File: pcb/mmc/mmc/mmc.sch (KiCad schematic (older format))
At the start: 1 part

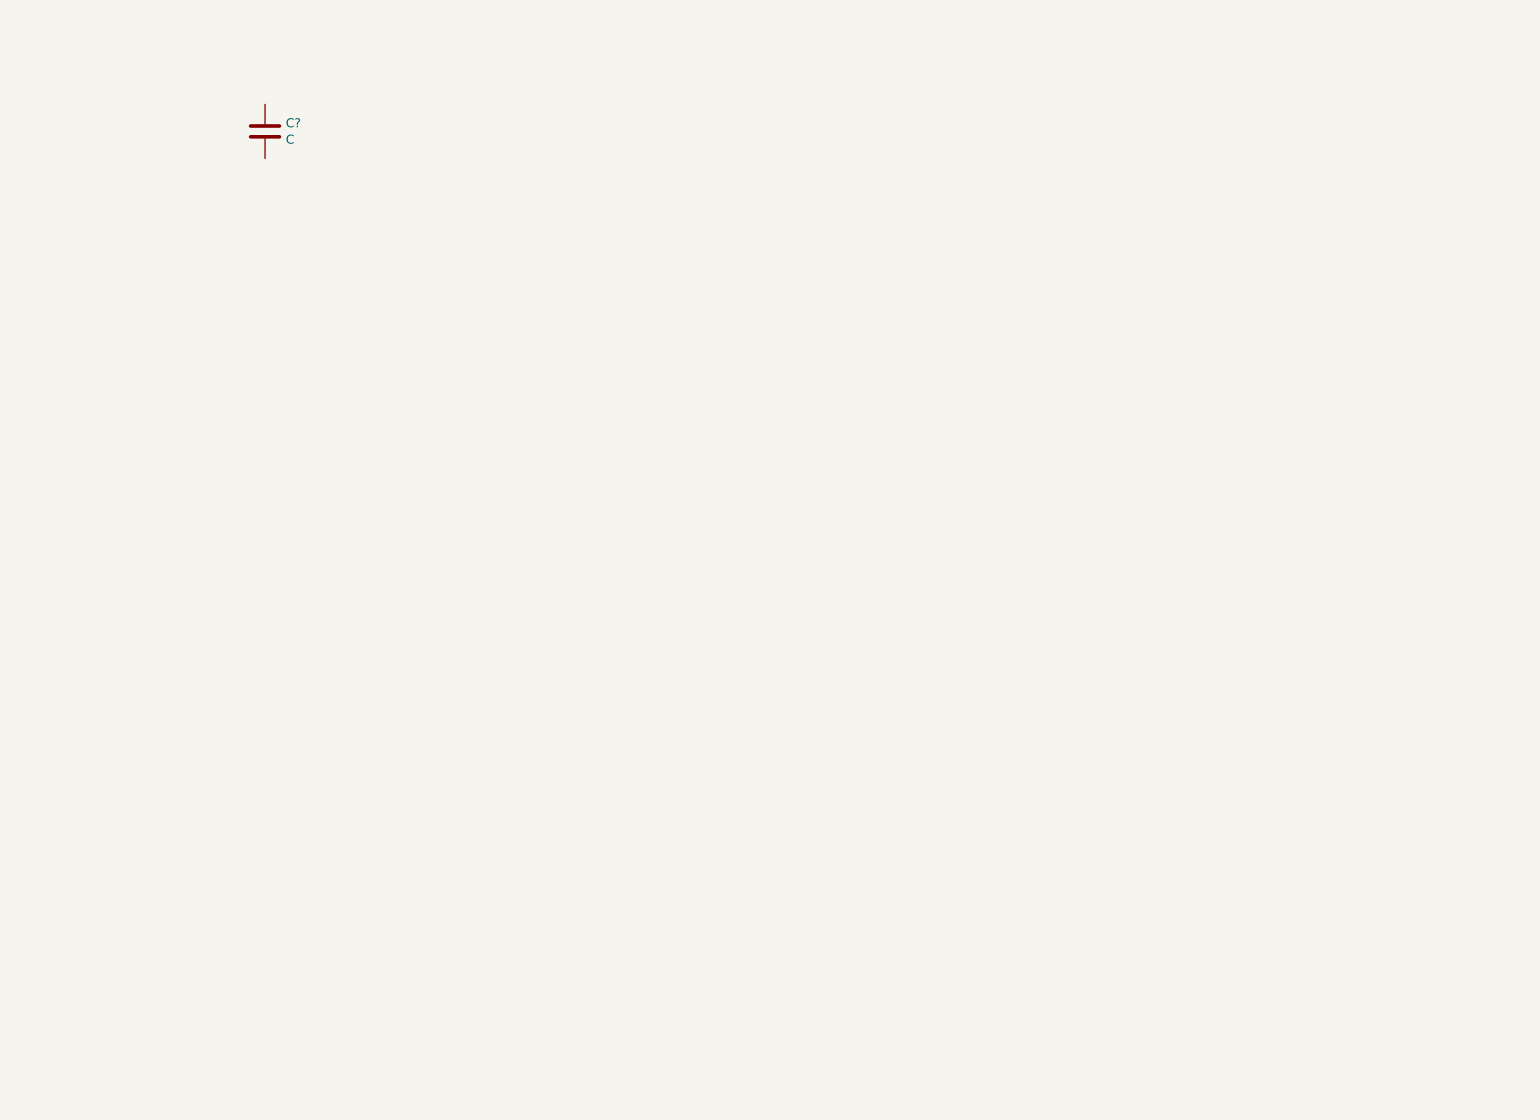
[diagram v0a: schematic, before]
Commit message: finished power and MMC PCBs and created gerbers
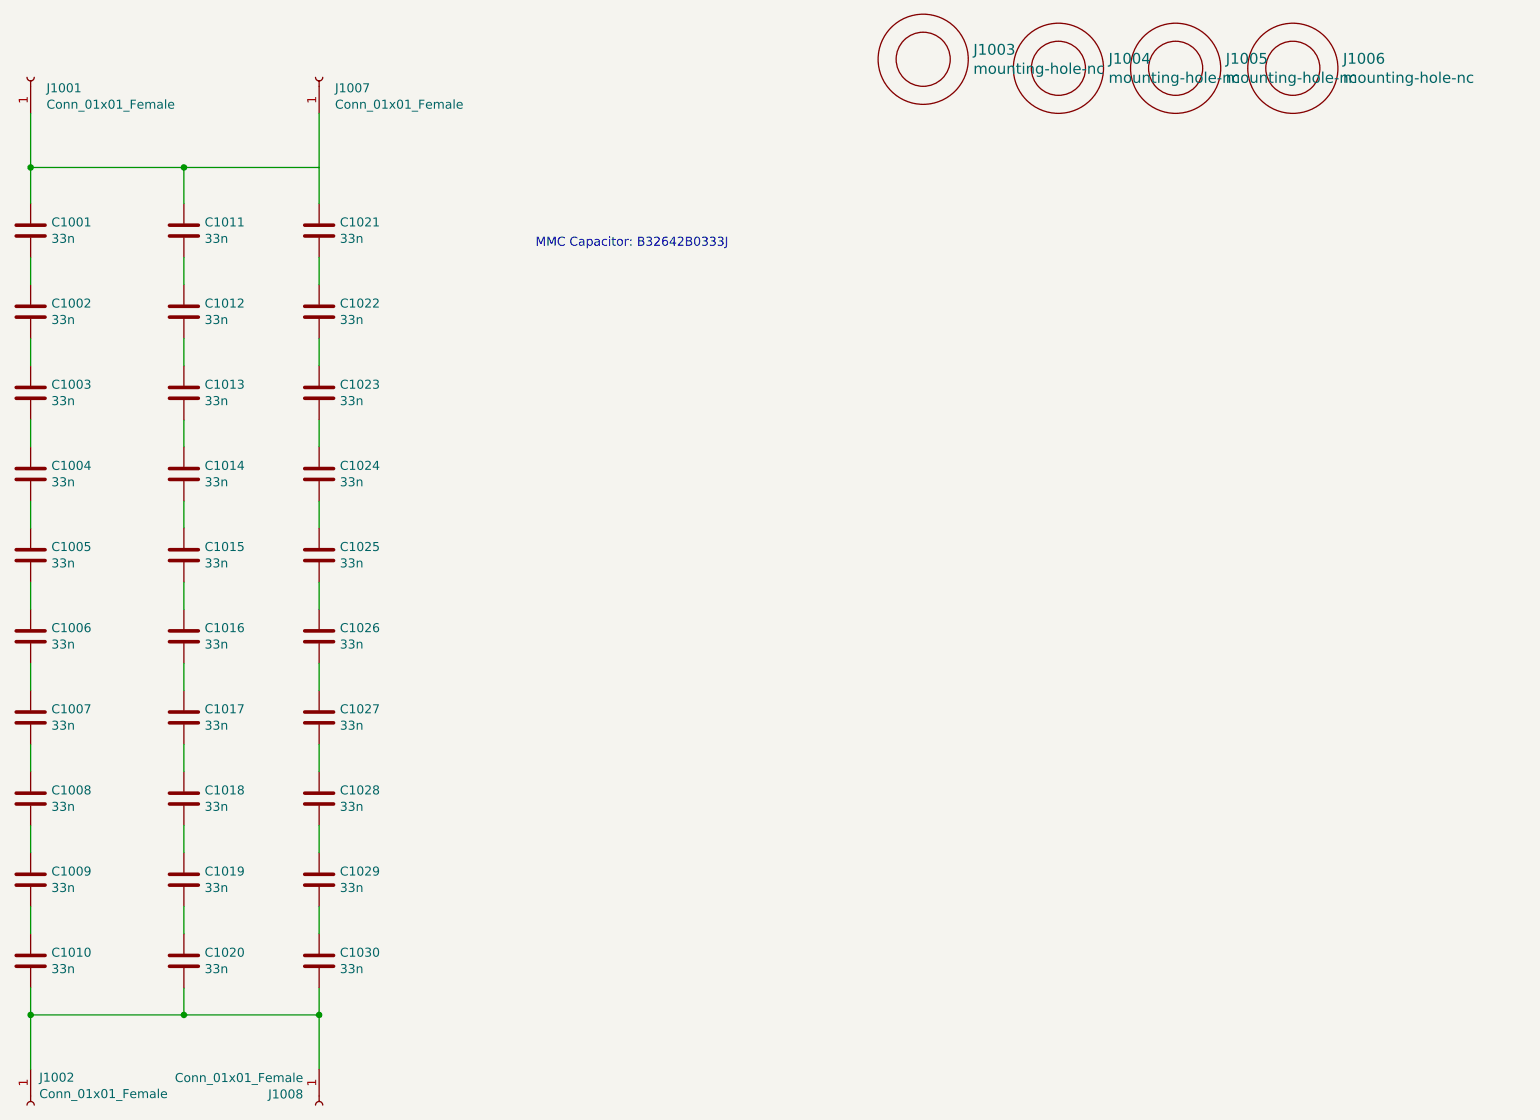
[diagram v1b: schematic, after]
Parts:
- added C1002, C1003, C1004, C1005, C1006, C1007, C1008, C1009, C1010, C1011, C1012, C1013, C1014, C1015, C1016, C1017, C1018, C1019, C1020, C1021, C1022, C1023, C1024, C1025, C1026, C1027, C1028, C1029, C1030: 33n, Capacitor_THT:C_Rect_L18.0mm_W7.0mm_P15.00mm_FKS3_FKP3, symbol Device:C
- added J1001, J1002, J1007, J1008: Conn_01x01_Female, wbraun_smd:7693-term, symbol Connector:Conn_01x01_Female
- added J1003, J1004, J1005, J1006: mounting-hole-nc, wbraun_smd:M3-mounting-hole-insulated, symbol wbraun_ic_lib:mounting-hole-nc
- C1001: renamed from C?; value C -> 33n; footprint (none) -> Capacitor_THT:C_Rect_L18.0mm_W7.0mm_P15.00mm_FKS3_FKP3
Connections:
- net at C1001.1: now also C1011.1, C1021.1, J1001.1 (Pin_1), J1007.1 (Pin_1)
- net at C1001.2: now also C1002.1
- new net: C1002.2, C1003.1
- new net: C1003.2, C1004.1
- new net: C1004.2, C1005.1
- new net: C1005.2, C1006.1
- new net: C1006.2, C1007.1
- new net: C1007.2, C1008.1
- new net: C1008.2, C1009.1
- new net: C1009.2, C1010.1
- new net: C1010.2, C1020.2, C1030.2, J1002.1 (Pin_1), J1008.1 (Pin_1)
- new net: C1011.2, C1012.1
- new net: C1012.2, C1013.1
- new net: C1013.2, C1014.1
- new net: C1014.2, C1015.1
- new net: C1015.2, C1016.1
- new net: C1016.2, C1017.1
- new net: C1017.2, C1018.1
- new net: C1018.2, C1019.1
- new net: C1019.2, C1020.1
- new net: C1021.2, C1022.1
- new net: C1022.2, C1023.1
- new net: C1023.2, C1024.1
- new net: C1024.2, C1025.1
- new net: C1025.2, C1026.1
- new net: C1026.2, C1027.1
- new net: C1027.2, C1028.1
- new net: C1028.2, C1029.1
- new net: C1029.2, C1030.1
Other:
- note added: "MMC Capacitor: B32642B0333J"
- moved on the sheet: C1001
